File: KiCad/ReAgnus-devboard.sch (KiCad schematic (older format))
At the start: 12 parts, among them J1 Barrel_Jack_Switch, J2 Conn_02x01, J3 Conn_01x01, J4 Conn_01x01, J5 Conn_01x01, J6 Conn_01x01, SW1 SW_SPDT, U1 PLCC-84-Plug, U2 ReAgnus_8375_socket, U3 Agnus_8375_socket

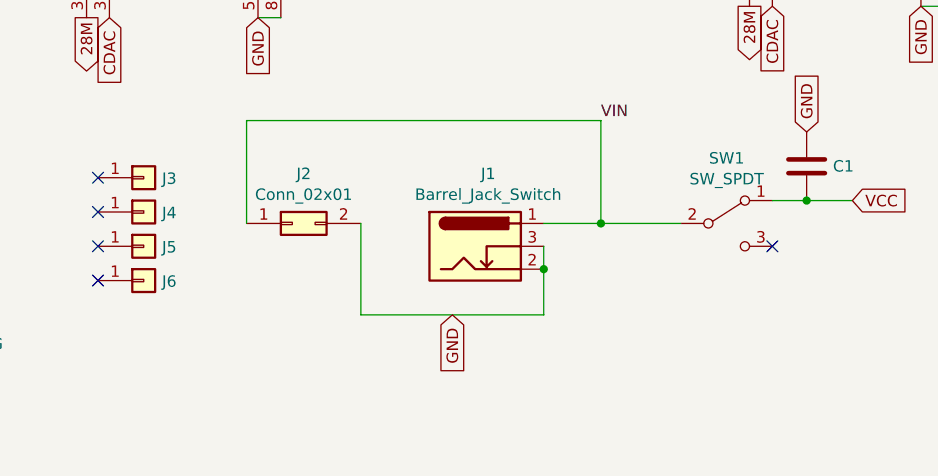
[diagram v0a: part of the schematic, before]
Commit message: Added a microUSB jack for power supply
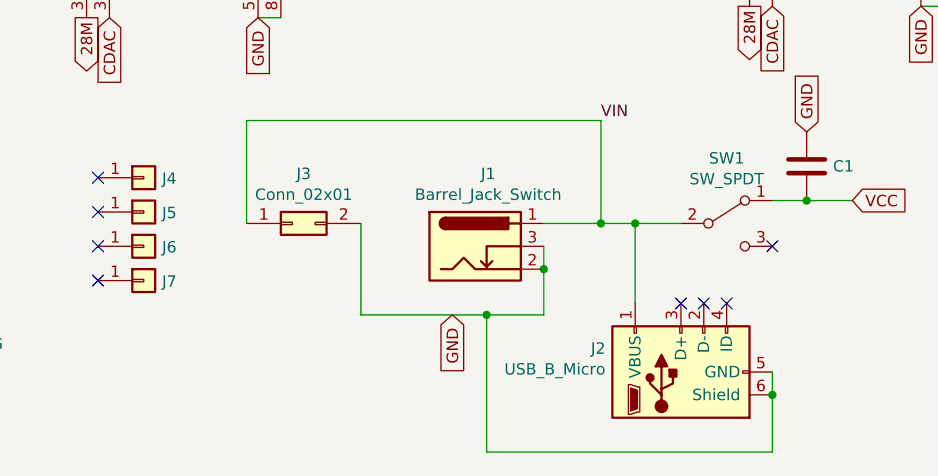
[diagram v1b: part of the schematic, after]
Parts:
- added J2: USB_B_Micro, Agnus:USB_Micro-B_Unknown_5s_SMT, symbol Connector:USB_B_Micro
- renumbered J2 to J3, J3 to J4, J4 to J5, J5 to J6, J6 to J7
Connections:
- net GND: now also J2.5 (GND), J2.6 (Shield)
- net VIN: now also J2.1 (VBUS)
- no-connect marks 5 -> 8
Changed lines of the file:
@@
 AS
 $Comp
-L Connector_Generic:Conn_01x01 J3
+L Connector_Generic:Conn_01x01 J4
 U 1 1 60D1FBEB
 P 2000 6450
-F 0 "J3" H 2080 6446 50  0000 L CNN
+F 0 "J4" H 2080 6446 50  0000 L CNN
 F 1 "Conn_01x01" H 2080 6401 50  0001 L CNN
 F 2 "Connector_PinHeader_2.54mm:PinHeader_1x01_P2.54mm_Vertical" H 2000 6450 50  0001 C CNN
@@
 $EndComp
 $Comp
-L Connector_Generic:Conn_01x01 J4
+L Connector_Generic:Conn_01x01 J5
 U 1 1 60D20CDD
 P 2000 6600
-F 0 "J4" H 2080 6596 50  0000 L CNN
+F 0 "J5" H 2080 6596 50  0000 L CNN
 F 1 "Conn_01x01" H 2080 6551 50  0001 L CNN
 F 2 "Connector_PinHeader_2.54mm:PinHeader_1x01_P2.54mm_Vertical" H 2000 6600 50  0001 C CNN
@@
 $EndComp
 $Comp
-L Connector_Generic:Conn_01x01 J5
+L Connector_Generic:Conn_01x01 J6
 U 1 1 60D21648
 P 2000 6750
-F 0 "J5" H 2080 6746 50  0000 L CNN
+F 0 "J6" H 2080 6746 50  0000 L CNN
 F 1 "Conn_01x01" H 2080 6701 50  0001 L CNN
 F 2 "Connector_PinHeader_2.54mm:PinHeader_1x01_P2.54mm_Vertical" H 2000 6750 50  0001 C CNN
@@
 $EndComp
 $Comp
-L Connector_Generic:Conn_01x01 J6
+L Connector_Generic:Conn_01x01 J7
 U 1 1 60D21D5E
 P 2000 6900
-F 0 "J6" H 2080 6896 50  0000 L CNN
+F 0 "J7" H 2080 6896 50  0000 L CNN
 F 1 "Conn_01x01" H 2080 6851 50  0001 L CNN
 F 2 "Connector_PinHeader_2.54mm:PinHeader_1x01_P2.54mm_Vertical" H 2000 6900 50  0001 C CNN
@@
 $EndComp
 $Comp
-L Connector_Generic:Conn_02x01 J2
+L Connector_Generic:Conn_02x01 J3
 U 1 1 60E54D12
 P 2650 6650
-F 0 "J2" H 2700 6867 50  0000 C CNN
+F 0 "J3" H 2700 6867 50  0000 C CNN
 F 1 "Conn_02x01" H 2700 6776 50  0000 C CNN
 F 2 "Connector_PinHeader_2.54mm:PinHeader_2x01_P2.54mm_Vertical" H 2650 6650 50  0001 C CNN
@@
 	2950 6650 2950 7050
 Wire Wire Line
-	2950 7050 3750 7050
+	2950 7050 3500 7050
 Wire Wire Line
 	3750 7050 3750 6850
@@
 $EndComp
 Wire Wire Line
-	4350 6650 4000 6650
+	4350 6650 4150 6650
 Connection ~ 4000 6650
 NoConn ~ 4750 6750
@@
 Wire Wire Line
 	9000 4900 9250 4900
+$Comp
+L Connector:USB_B_Micro J2
+U 1 1 6138898E
+P 4350 7300
+F 0 "J2" V 4453 7630 50  0000 L CNN
+F 1 "USB_B_Micro" V 4362 7630 50  0000 L CNN
+F 2 "Agnus:USB_Micro-B_Unknown_5s_SMT" H 4500 7250 50  0001 C CNN
+F 3 "~" H 4500 7250 50  0001 C CNN
+	1    4350 7300
+	0    -1   -1   0
+$EndComp
+Wire Wire Line
+	4750 7300 4750 7400
+Wire Wire Line
+	4750 7650 3500 7650
+Wire Wire Line
+	3500 7650 3500 7050
+Connection ~ 4750 7400
+Wire Wire Line
+	4750 7400 4750 7650
+Connection ~ 3500 7050
+Wire Wire Line
+	3500 7050 3750 7050
+NoConn ~ 4550 7000
+NoConn ~ 4450 7000
+NoConn ~ 4350 7000
+Wire Wire Line
+	4150 7000 4150 6650
+Connection ~ 4150 6650
+Wire Wire Line
+	4150 6650 4000 6650
 $EndSCHEMATC
